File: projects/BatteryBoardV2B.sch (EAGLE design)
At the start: 225 parts, among them M1 BSO201SP, SW1 BTS50015-1TAD, SW2 BTS50015-1TAD, T1 AD590FLATPACK, T2 AD590FLATPACK, T3 AD590FLATPACK, T4 AD590FLATPACK, U1 TCA9535PWR, U10 LT1962-3, U11 LT1962-3, U12 LTC4411, U13 LTC4411, U14 LTC4121, U15 VNS3NV04DP-E, U16 LTC4121, U17 VNS3NV04DP-E, U18 AD8418, U19 AD8418, U2 AD7991-0, U3 LTC4412MPS6, U4 LTC4121-4.2, U5 LTC4121-4.2, U6 LC05111C13MTTTG, U7 LC05111C13MTTTG, U8 AD8418, U9 AD8418

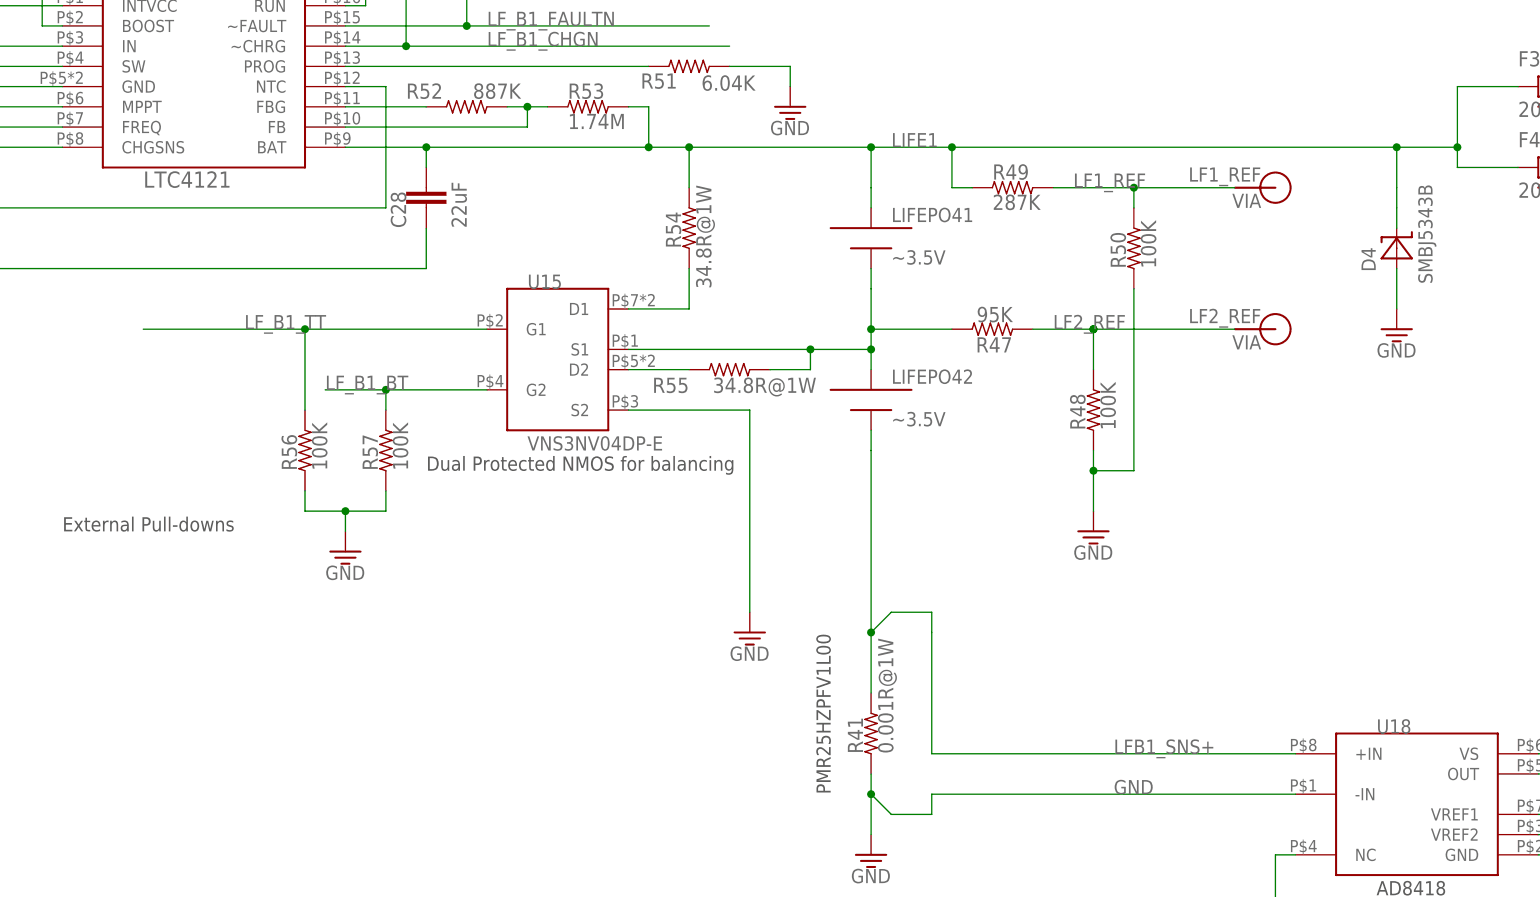
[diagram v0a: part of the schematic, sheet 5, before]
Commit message: Updating schematic for battery board, adding schematic for flight configuration
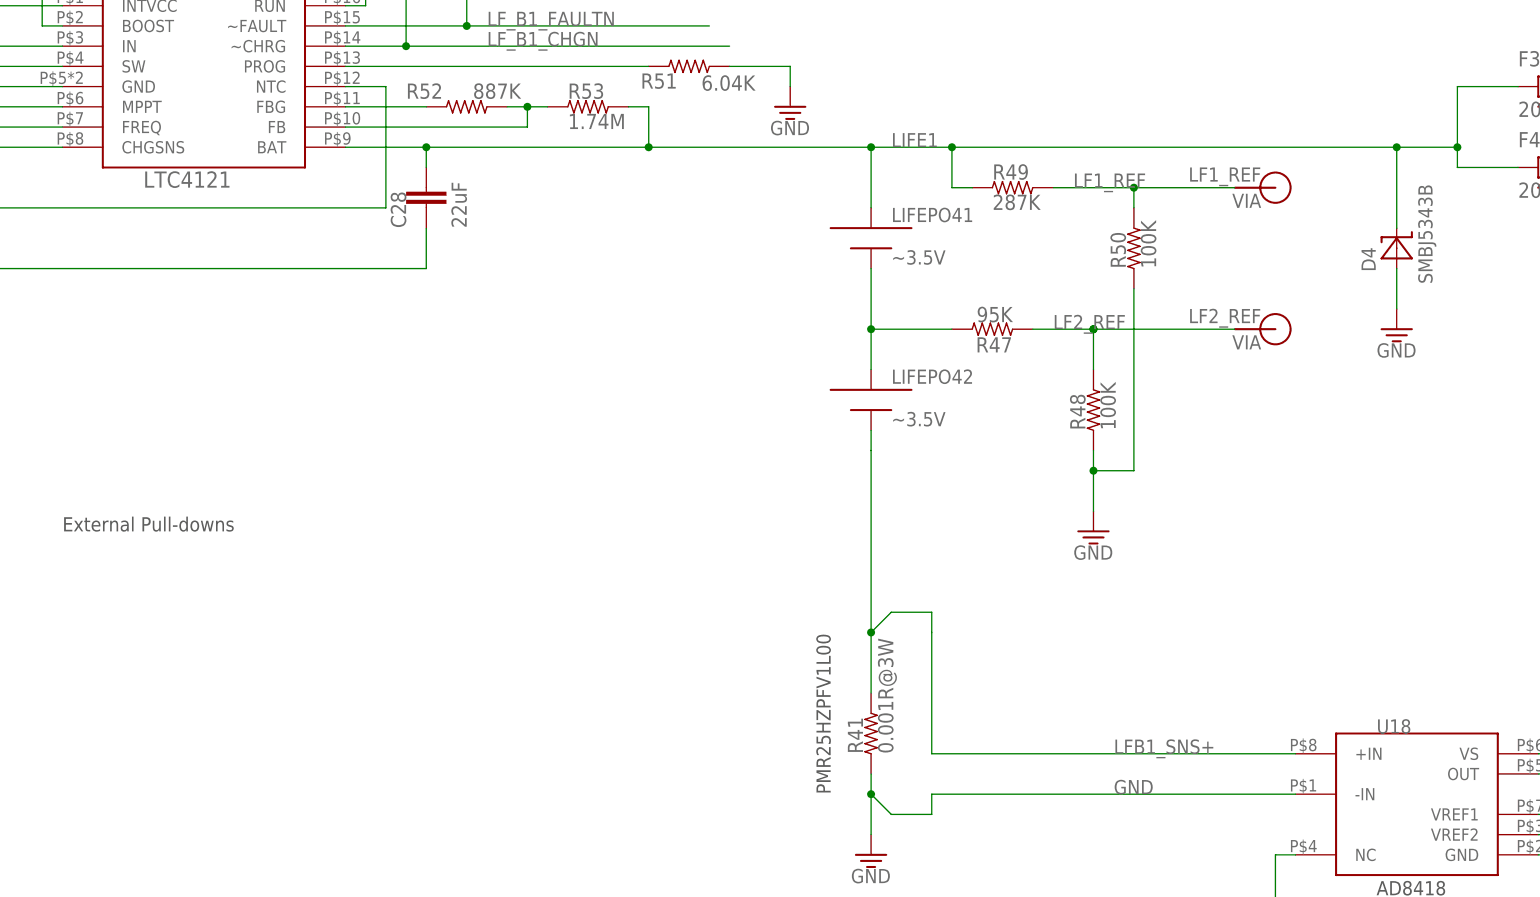
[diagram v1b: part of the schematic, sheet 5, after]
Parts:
- removed R5: 0R, BrownSpaceEngineering:RES0805
- removed R54, R55, R72, R73: 34.8R@1W, BrownSpaceEngineering:RES1210
- removed R56, R57, R74, R75: 100K, BrownSpaceEngineering:RES0805
- removed U15, U17: VNS3NV04DP-E, BrownSpaceEngineering:VNS3NV04DP-E
- R41, R59: value 0.001R@1W -> 0.001R@3W
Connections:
- removed net N$24: R54.1, U15.D1
- removed net N$25: R55.2, U15.D2
- removed net N$42: R72.1, U17.D1
- removed net N$43: R73.2, U17.D2
- net GND: no longer R56.1, R57.1, R74.1, R75.1, U15.S2, U17.S2
- net LF_B1_BT: no longer R57.2, U15.G2
- net LF_B1_TT: no longer R56.2, U15.G1
- net LF_B2_BT: no longer R75.2, U17.G2
- net LF_B2_TT: no longer R74.2, U17.G1
- net LIFE1: no longer R54.2
- net LIFE2: no longer R55.1, U15.S1
- net LIFE3: no longer R72.2
- net LIFE4: no longer R73.1, U17.S1
- net SP_C: no longer R5.1
- net SP_OUT: no longer R5.2
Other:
- note removed: "Dual Protected NMOS for balancing"
